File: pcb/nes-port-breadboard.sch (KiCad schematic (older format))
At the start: 2 parts, among them J1 Conn_01x07, J2 NES_Port_Male

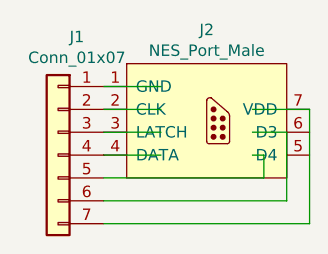
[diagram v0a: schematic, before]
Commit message: Update mounting holes
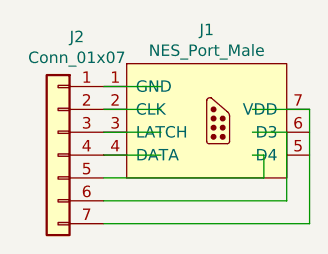
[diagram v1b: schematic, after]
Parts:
- renumbered J2 to J1, J1 to J2
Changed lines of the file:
@@
 Title "NES Port Breadboard Adapter"
 Date "2021-06-09"
-Rev "1"
+Rev "1.0"
 Comp ""
 Comment1 ""
@@
 $EndDescr
 $Comp
-L nes-port-breadboard:NES_Port_Male J2
+L nes-port-breadboard:NES_Port_Male J1
 U 1 1 60C605E6
 P 5350 3250
-F 0 "J2" H 5350 3648 50  0000 C CNN
+F 0 "J1" H 5350 3648 50  0000 C CNN
 F 1 "NES_Port_Male" H 5350 3557 50  0000 C CNN
 F 2 "nes-port-breadboard:NES_Port_Male_Horizontal" H 5350 3250 50  0001 C CNN
@@
 $EndComp
 $Comp
-L Connector_Generic:Conn_01x07 J1
+L Connector_Generic:Conn_01x07 J2
 U 1 1 60C61DBB
 P 4700 3400
-F 0 "J1" H 4618 3917 50  0000 C CNN
+F 0 "J2" H 4618 3917 50  0000 C CNN
 F 1 "Conn_01x07" H 4618 3826 50  0000 C CNN
 F 2 "Connector_PinHeader_2.54mm:PinHeader_1x07_P2.54mm_Vertical" H 4700 3400 50  0001 C CNN
